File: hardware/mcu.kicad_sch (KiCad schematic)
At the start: 41 parts, among them J1 SWD header, J3 I2C header, J5 Debug UART Header, J8 Modem UART Header, U1 AT25SF081-SSHD-B, U2 STM32L552CEU6, U3 MCP9808, Y1 ECS-160-9-37-CKM-TR3, Y2 ABS05-32.768KHZ-9-T

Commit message: HW: Continue developing
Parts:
- removed U2: STM32L552CEU6, Package_DFN_QFN:QFN-48-1EP_7x7mm_P0.5mm_EP5.6x5.6mm, symbol MCU_ST_STM32L5:STM32L552CEUx
- added JP1, JP2, JP3, JP4, JP5: SolderJumper_2_Open, Jumper:SolderJumper-2_P1.3mm_Open_RoundedPad1.0x1.5mm, symbol Jumper:SolderJumper_2_Open
- added U7: STM32L552CEU6, Package_DFN_QFN:QFN-48-1EP_7x7mm_P0.5mm_EP5.6x5.6mm_ThermalVias, symbol STM32L552CEU6:STM32L552CEUx
- J3: value I2C header -> Conn_01x04; footprint (none) -> Connector_PinHeader_2.54mm:PinHeader_1x04_P2.54mm_Vertical; Digi-Key Part Number (none) -> S1011EC-04-ND; Manufacturer (none) -> Sullins Connector Solutions; Manufacturer Part Number (none) -> PRPC004SAAN-RC
- J5: value Debug UART Header -> Conn_01x06; footprint (none) -> Connector_PinHeader_2.54mm:PinHeader_1x06_P2.54mm_Vertical; Digi-Key Part Number (none) -> S1011EC-06-ND; Manufacturer (none) -> Sullins Connector Solutions; Manufacturer Part Number (none) -> PRPC006SAAN-RC
- J8: value Modem UART Header -> Conn_01x06; footprint (none) -> Connector_PinHeader_2.54mm:PinHeader_1x06_P2.54mm_Vertical; Digi-Key Part Number (none) -> S1011EC-06-ND; Manufacturer (none) -> Sullins Connector Solutions; Manufacturer Part Number (none) -> PRPC006SAAN-RC
- R30, R31: footprint (none) -> perfect_footprints:0402_1005_perfect; Digi-Key Part Number (none) -> 311-22.0LRCT-ND; Manufacturer (none) -> YAGEO; Manufacturer Part Number (none) -> RC0402FR-0722RL
- U1: footprint Package_CSP:WLCSP-8_1.58x1.63x0.35mm_Layout3x5_P0.35x0.4mm_Ball0.25mm_Pad0.25mm_NSMD -> Package_SO:SOIC-8_3.9x4.9mm_P1.27mm
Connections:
- net +3.3V: now also J8.1 (Pin_1), U7.1 (VBAT), U7.24 (VDD), U7.36 (VDD), U7.48 (VDD); no longer J8.3 (Pin_3)
- net DBG_UART_RX: now also U7.13 (PA3)
- net DBG_UART_TX: now also U7.12 (PA2)
- net EXT_FLASH_CLK: now also U7.21 (PB10)
- net EXT_FLASH_IO0: now also U7.19 (PB1)
- net EXT_FLASH_IO1: now also U7.18 (PB0)
- net EXT_FLASH_IO2: now also U7.17 (PA7)
- net EXT_FLASH_IO3: now also U7.16 (PA6)
- net EXT_FLASH_NCS: now also U7.22 (PB11)
- net GND: now also J8.2 (Pin_2), U7.23 (VSS), U7.35 (VSS), U7.47 (VSS), U7.49 (VSS), U7.8 (VSSA); no longer J8.1 (Pin_1)
- net HSE_IN: now also U7.5 (PH0)
- net HSE_OUT: now also U7.6 (PH1)
- net I2C_SCL: now also U7.26 (PB13)
- net I2C_SDA: now also U7.27 (PB14)
- net LSE_IN: now also U7.3 (PC14)
- net LSE_OUT: now also U7.4 (PC15)
- net MODEM_RX: now also JP2.2 (B); no longer R31.1
- net MODEM_TX: now also JP1.2 (B); no longer R30.1
- net NRST: now also U7.7 (NRST)
- net SWCLK: now also U7.37 (PA14)
- net SWDIO: now also U7.34 (PA13)
- net SWO: now also U7.39 (PB3)
- net TEMP_ALERT: now also U7.25 (PB12)
- net USB_DN: now also U7.32 (PA11)
- net USB_DP: now also U7.33 (PA12)
- net at R10.2, R12.1: now also U7.14 (PA4)
- net at C16.1, C17.1, FB1.1: now also U7.9 (VDDA)
- net at R7.1: now also U7.30 (PA9)
- net at R31.2: now also U7.43 (PB7)
- net at R6.1: now also U7.29 (PA8)
- net at R4.2, R5.1: now also U7.15 (PA5)
- net at R8.1: now also U7.31 (PA10)
- net at R30.2: now also U7.42 (PB6)
- new net: JP2.1 (A), R31.1
- new net: JP1.1 (A), R30.1
- new net: JP4.1 (A), U7.40 (PB4)
- new net: JP3.1 (A), U7.44 (PH3)
- new net: JP5.1 (A), U7.41 (PB5)
- new net ~{MODEM_IRQ}: JP3.2 (B)
- new net ~{MODEM_PWR_EN}: JP4.2 (B)
- new net ~{MODEM_RST}: JP5.2 (B)
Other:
- moved on the sheet: C1, C11, C12, C13, C14, C15, C16, C17, C18, C2, C3, C4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

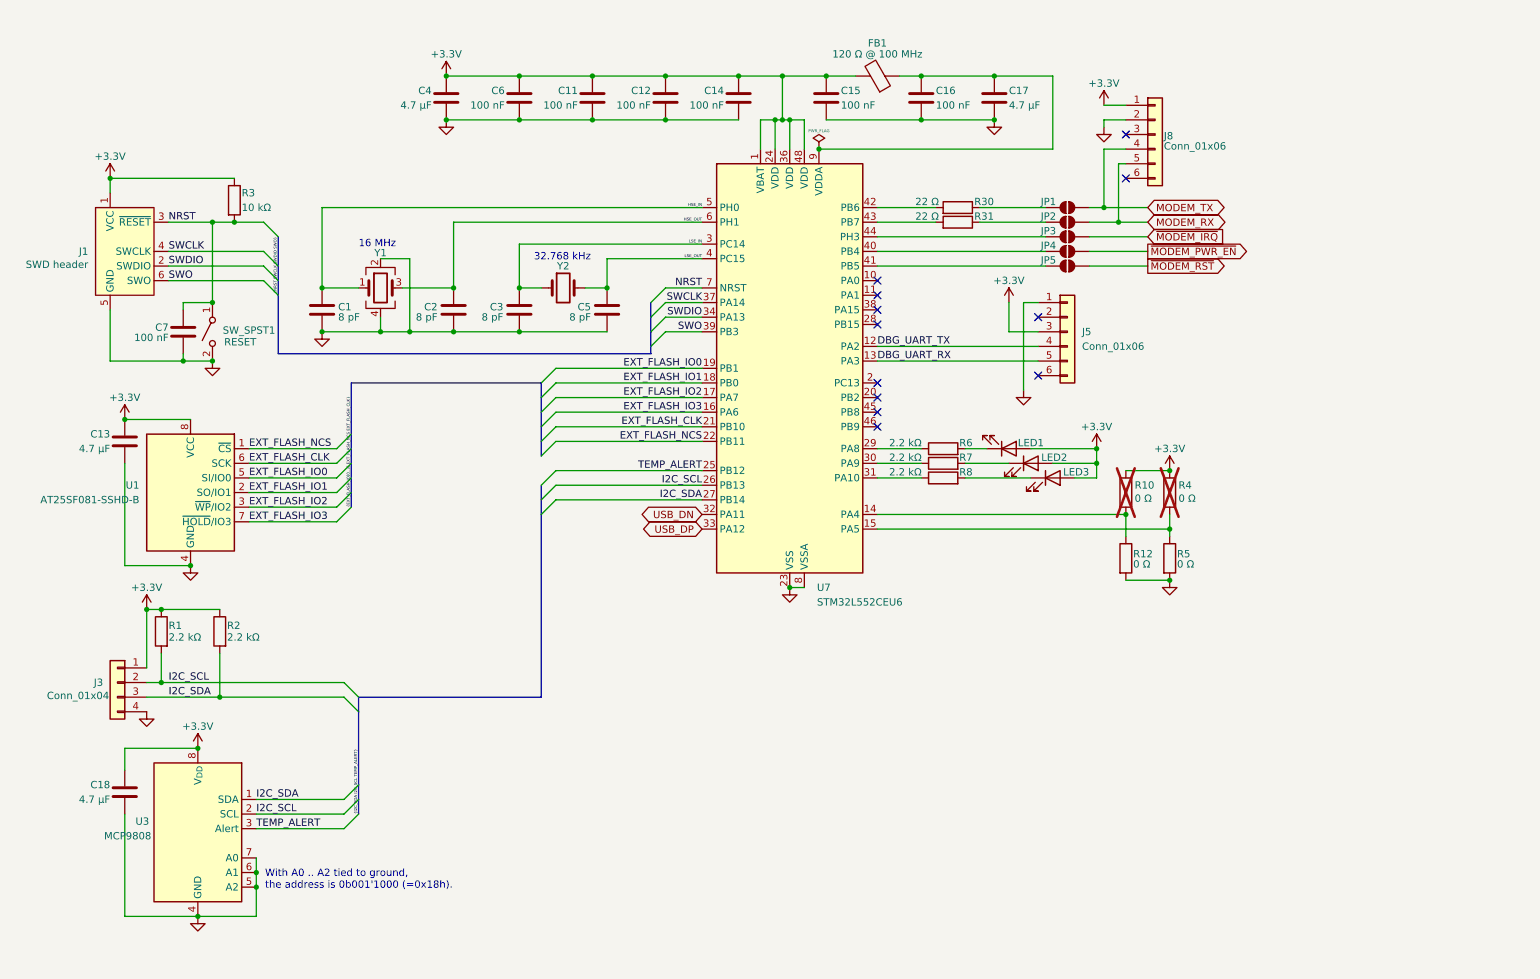
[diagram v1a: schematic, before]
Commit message: HW: Develop further
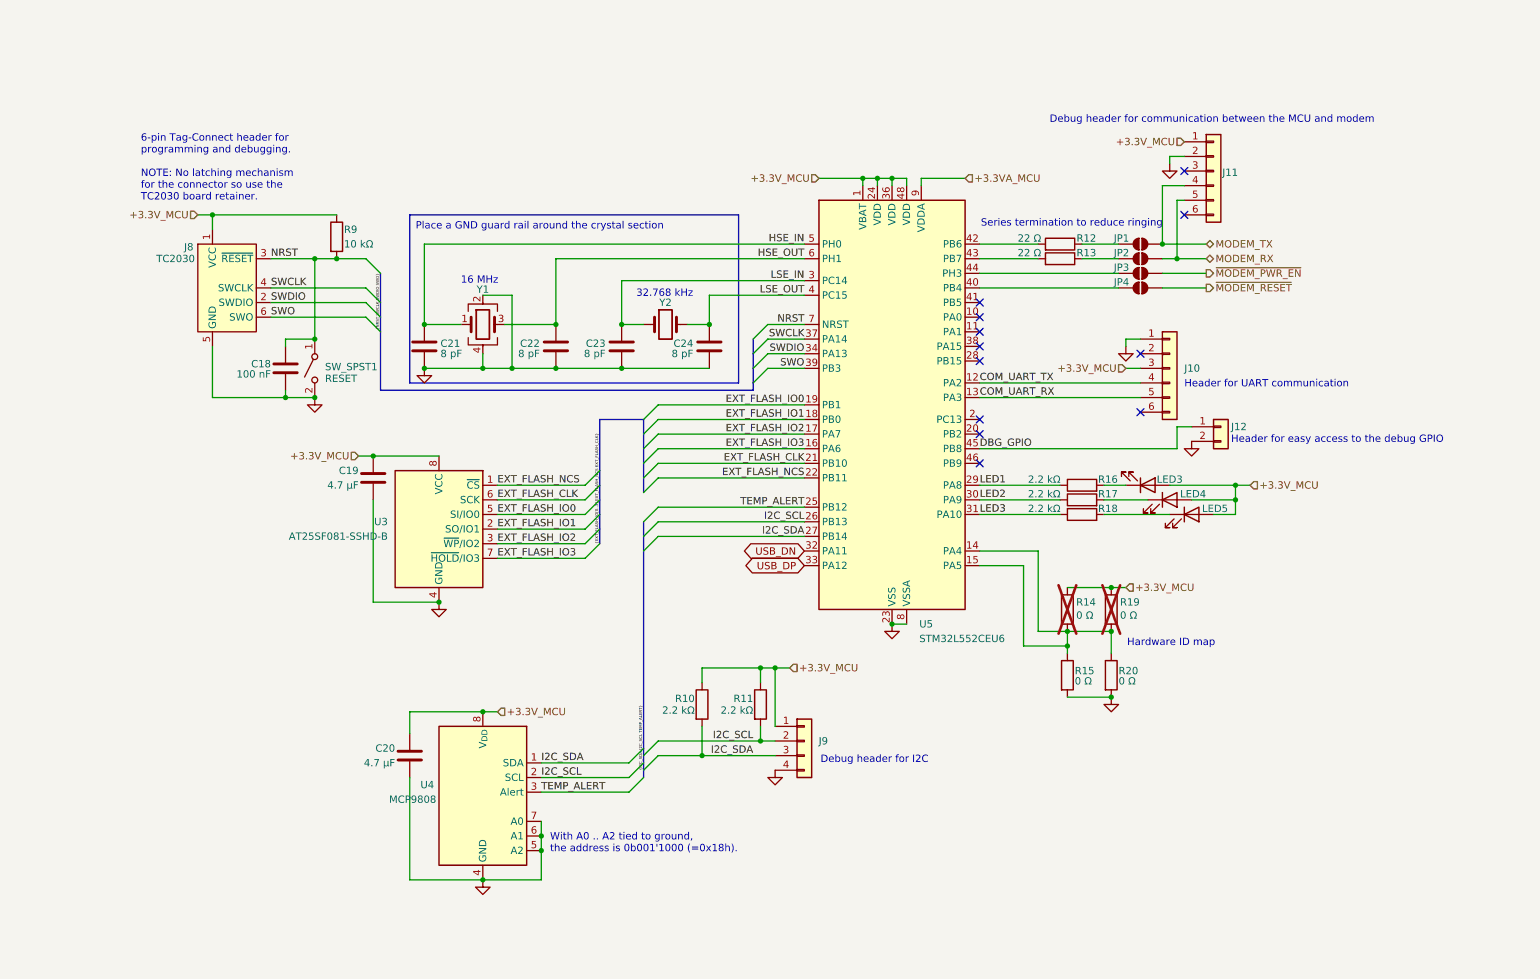
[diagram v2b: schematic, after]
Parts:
- removed C11, C12, C14, C15, C16, C6: 100 nF, perfect_footprints:0402_1005_perfect, symbol Device:C
- removed C17, C4: 4.7 µF, Capacitor_SMD:C_0603_1608Metric, symbol Device:C
- removed FB1: 120 Ω @ 100 MHz, Resistor_SMD:R_0603_1608Metric, symbol Device:FerriteBead
- removed JP3: SolderJumper_2_Open, Jumper:SolderJumper-2_P1.3mm_Open_RoundedPad1.0x1.5mm, symbol Jumper:SolderJumper_2_Open
- added J12: Conn_01x02, Connector_PinHeader_2.54mm:PinHeader_1x02_P2.54mm_Vertical, symbol Connector_Generic:Conn_01x02
- C18: renamed from C7; Digi-Key Part Number 1276-1002-1-ND -> 490-7998-1-ND; Manufacturer Samsung Electro-Mechanics -> Murata Electronics; Manufacturer Part Number CL05B104KP5NNNC -> GCM155R71C104KA55J
- J8: renamed from J1; value SWD header -> TC2030; Digi-Key Part Number (none) -> -; Manufacturer (none) -> -; Manufacturer Part Number (none) -> -
- JP1, JP2: Digi-Key Part Number (none) -> -; Manufacturer (none) -> -; Manufacturer Part Number (none) -> -
- JP3: renamed from JP4; Digi-Key Part Number (none) -> -; Manufacturer (none) -> -; Manufacturer Part Number (none) -> -
- JP4: renamed from JP5; Digi-Key Part Number (none) -> -; Manufacturer (none) -> -; Manufacturer Part Number (none) -> -
- renumbered C13 to C19, C18 to C20, C1 to C21, C2 to C22, C3 to C23, C5 to C24, J5 to J10, J8 to J11, J3 to J9, LED1 to LED3, LED2 to LED4, LED3 to LED5, R2 to R10, R1 to R11, R30 to R12, R31 to R13, R10 to R14, R12 to R15, R6 to R16, R7 to R17, R8 to R18, R4 to R19, R5 to R20, R3 to R9, U1 to U3, U3 to U4, U7 to U5
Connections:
- net GND: now also J12.2 (Pin_2)
- net at R14.2, R15.1, U5.14 (PA4): now also R19.2, R20.1, U5.15 (PA5)
- net +3.3VA_MCU: now reaches U5.9 (VDDA)
- net at JP3.1 (A): now also U5.44 (PH3); no longer U5.40 (PB4)
- net LED2: now reaches R17.1, U5.30 (PA9)
- net at JP4.1 (A): now also U5.40 (PB4); no longer U5.41 (PB5)
- net LED1: now reaches R16.1, U5.29 (PA8)
- net LED3: now reaches R18.1, U5.31 (PA10)
- net DBG_GPIO: now reaches U5.45 (PB8)
- net DBG_GPIO: now also J12.1 (Pin_1)
- net +3.3V renamed +3.3V_MCU
- net DBG_UART_RX renamed COM_UART_RX
- net DBG_UART_TX renamed COM_UART_TX
- net ~{MODEM_RST} renamed ~{MODEM_RESET}
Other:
- note added: "6-pin Tag-Connect header for programming and debugging. NOTE: No latching mechanism for the connector so use the TC2030 board retainer."
- note added: "Debug header for I2C"
- note added: "Debug header for communication between the MCU and modem"
- note added: "Hardware ID map"
- note added: "Header for UART communication"
- note added: "Header for easy access to the debug GPIO"
- note added: "Series termination to reduce ringing"
- moved on the sheet: C18, C19, C20, C21, C22, C23, C24, J10, J11, J8, J9, JP1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

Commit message: HW: Develop further
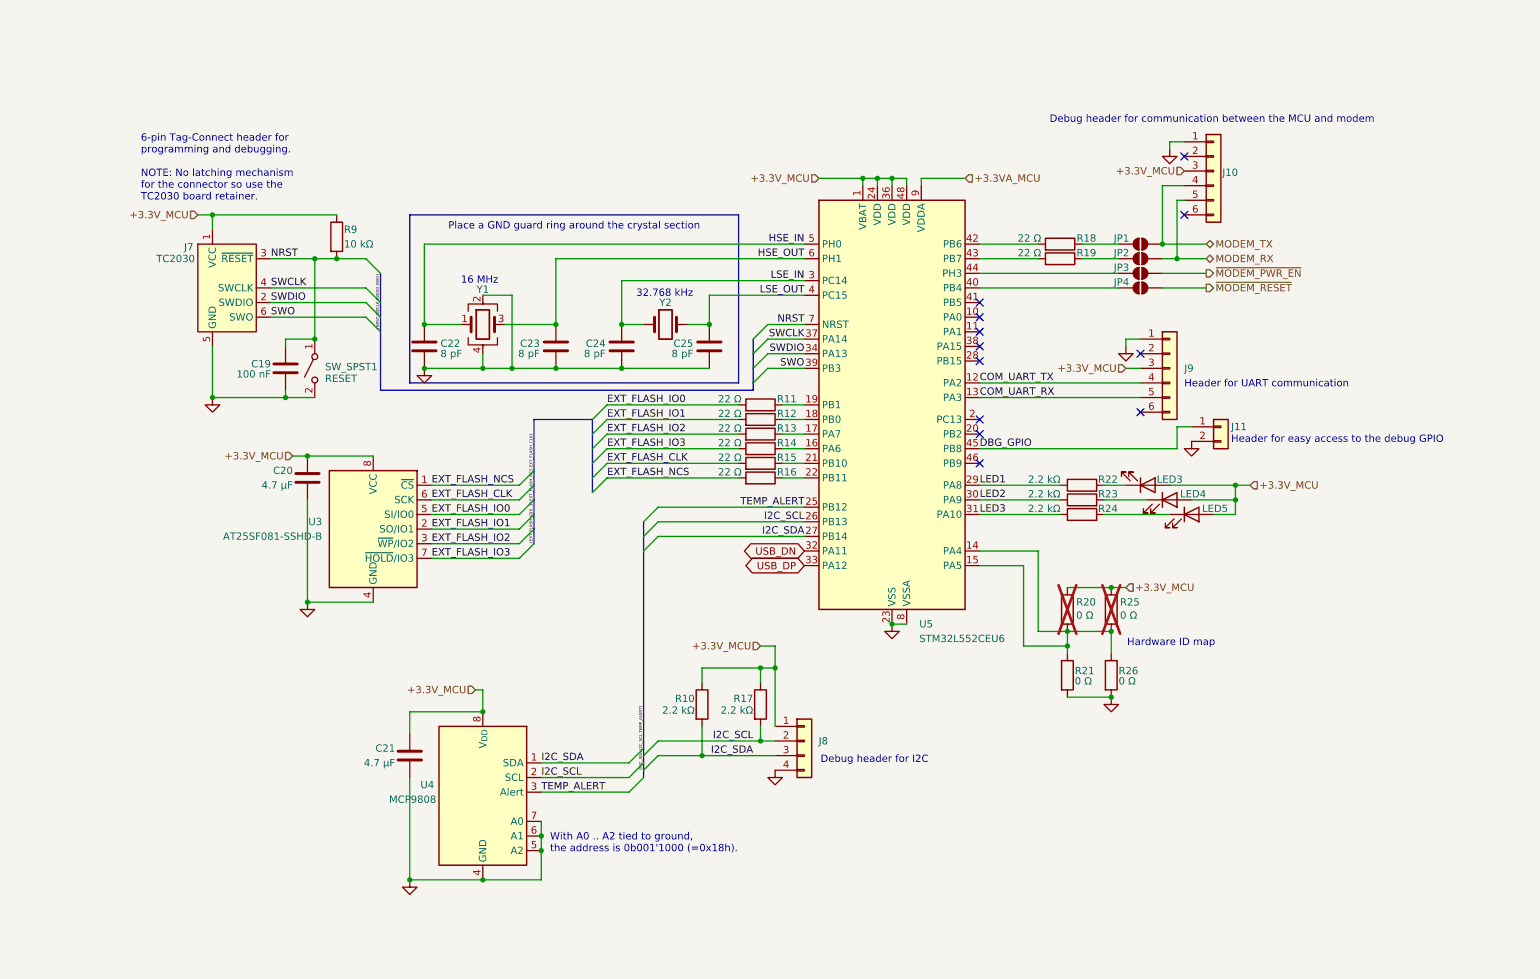
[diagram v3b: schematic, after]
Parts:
- added R11, R12, R13, R14, R15, R16: 22 Ω, perfect_footprints:0402_1005_perfect, symbol Device:R
- U5: footprint Package_DFN_QFN:QFN-48-1EP_7x7mm_P0.5mm_EP5.6x5.6mm_ThermalVias -> Package_DFN_QFN:QFN-48-1EP_7x7mm_P0.5mm_EP5.6x5.6mm
- renumbered C18 to C19, C19 to C20, C20 to C21, C21 to C22, C22 to C23, C23 to C24, C24 to C25, J11 to J10, J12 to J11, J8 to J7, J9 to J8, J10 to J9, R11 to R17, R12 to R18, R13 to R19, R14 to R20, R15 to R21, R16 to R22, R17 to R23, R18 to R24, R19 to R25, R20 to R26
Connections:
- net +3.3V_MCU: now also J10.3 (Pin_3); no longer J10.1 (Pin_1)
- net EXT_FLASH_CLK: now also R15.2; no longer U5.21 (PB10)
- net EXT_FLASH_IO0: now also R11.2; no longer U5.19 (PB1)
- net EXT_FLASH_IO1: now also R12.2; no longer U5.18 (PB0)
- net EXT_FLASH_IO2: now also R13.2; no longer U5.17 (PA7)
- net EXT_FLASH_IO3: now also R14.2; no longer U5.16 (PA6)
- net EXT_FLASH_NCS: now also R16.2; no longer U5.22 (PB11)
- net GND: now also J10.1 (Pin_1); no longer J10.2 (Pin_2)
- new net: R15.1, U5.21 (PB10)
- new net: R14.1, U5.16 (PA6)
- new net: R13.1, U5.17 (PA7)
- new net: R12.1, U5.18 (PB0)
- new net: R11.1, U5.19 (PB1)
- new net: R16.1, U5.22 (PB11)
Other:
- note removed: "Series termination to reduce ringing"
- moved on the sheet: C20, U3

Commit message: HW: Initial MCU layout
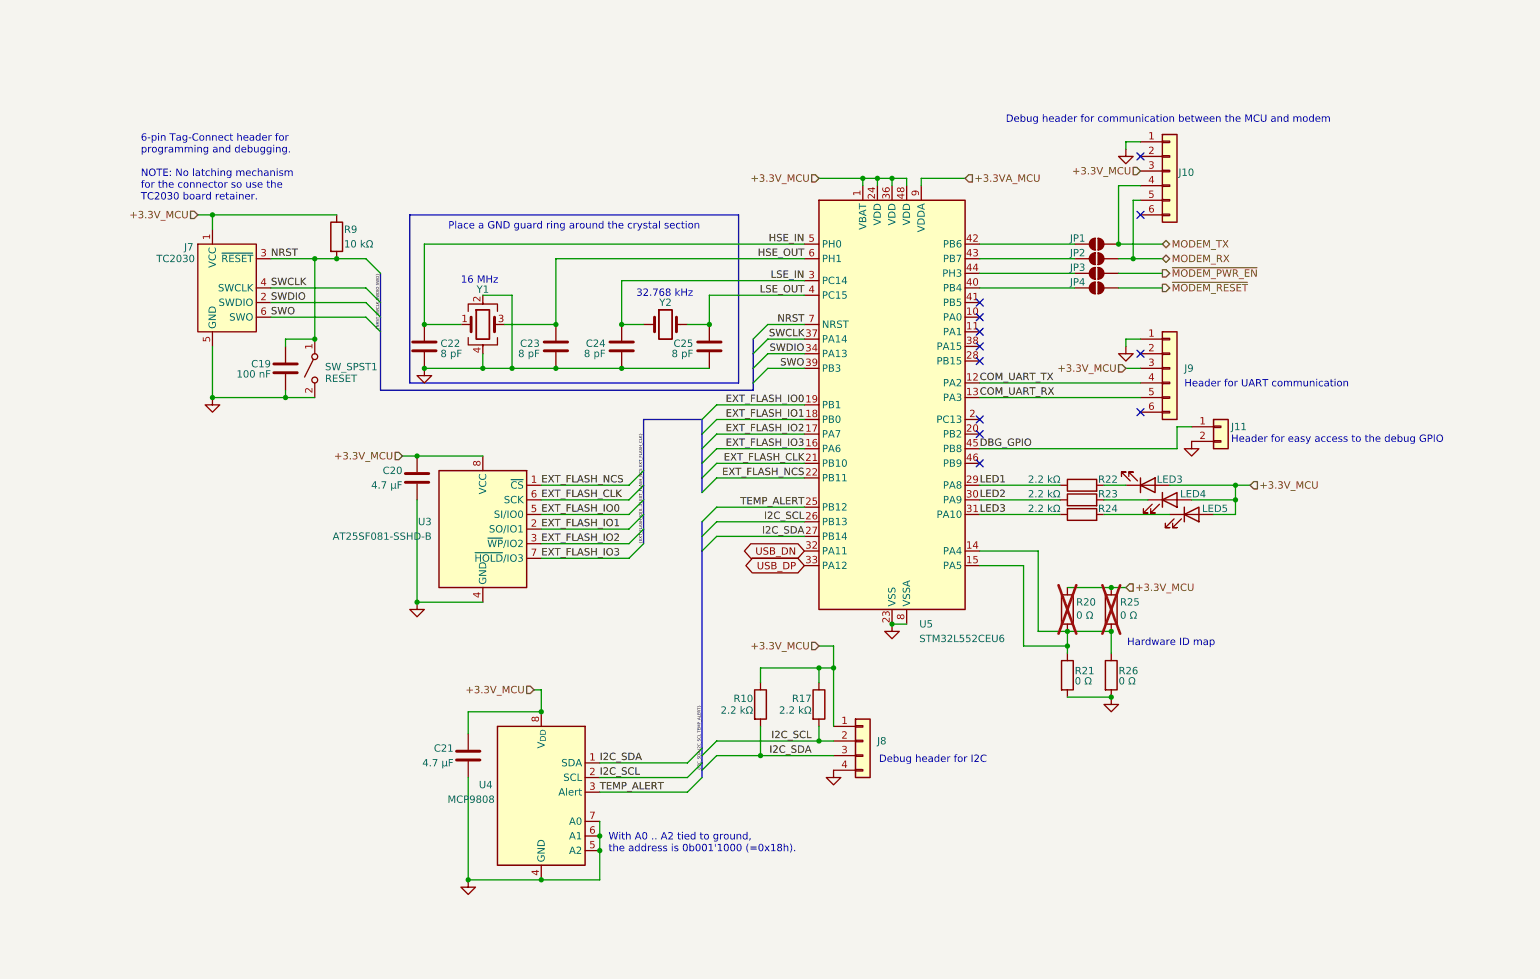
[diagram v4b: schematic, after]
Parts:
- removed R11, R12, R13, R14, R15, R16, R18, R19: 22 Ω, perfect_footprints:0402_1005_perfect, symbol Device:R
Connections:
- net EXT_FLASH_CLK: now also U5.21 (PB10)
- net EXT_FLASH_IO0: now also U5.19 (PB1)
- net EXT_FLASH_IO1: now also U5.18 (PB0)
- net EXT_FLASH_IO2: now also U5.17 (PA7)
- net EXT_FLASH_IO3: now also U5.16 (PA6)
- net EXT_FLASH_NCS: now also U5.22 (PB11)
- net at JP2.1 (A): now also U5.43 (PB7)
- net at JP1.1 (A): now also U5.42 (PB6)
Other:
- moved on the sheet: C20, C21, J10, J8, JP1, JP2, JP3, JP4, R10, R17, U3, U4

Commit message: HW: Finish laying out sections
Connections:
- net LED1 renamed LED_A
- net LED2 renamed LED_B
- net LED3 renamed LED_C
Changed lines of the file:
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@@
 		)
 	)
-	(label "LED2"
+	(label "LED_B"
 		(at 180.34 107.95 0)
 		(fields_autoplaced yes)
@@
 		)
 	)
-	(label "LED1"
+	(label "LED_A"
 		(at 180.34 105.41 0)
 		(fields_autoplaced yes)
@@
 		)
 	)
-	(label "LED3"
+	(label "LED_C"
 		(at 180.34 110.49 0)
 		(fields_autoplaced yes)
